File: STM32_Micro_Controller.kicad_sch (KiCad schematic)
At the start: 1 part, among them U1 STM32F103C8T6

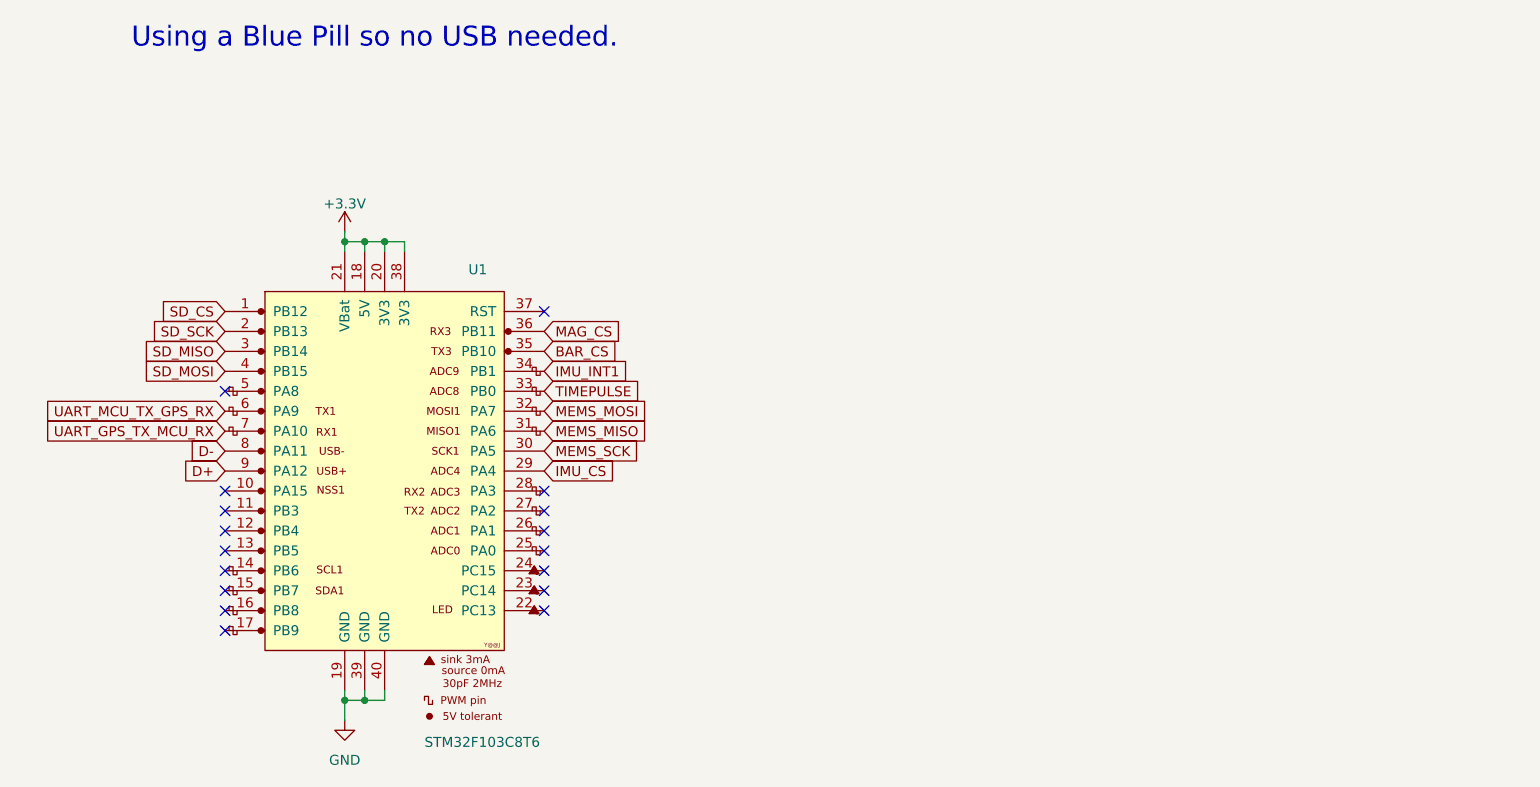
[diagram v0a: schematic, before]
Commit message: Finished the footprint for the Micro Controller
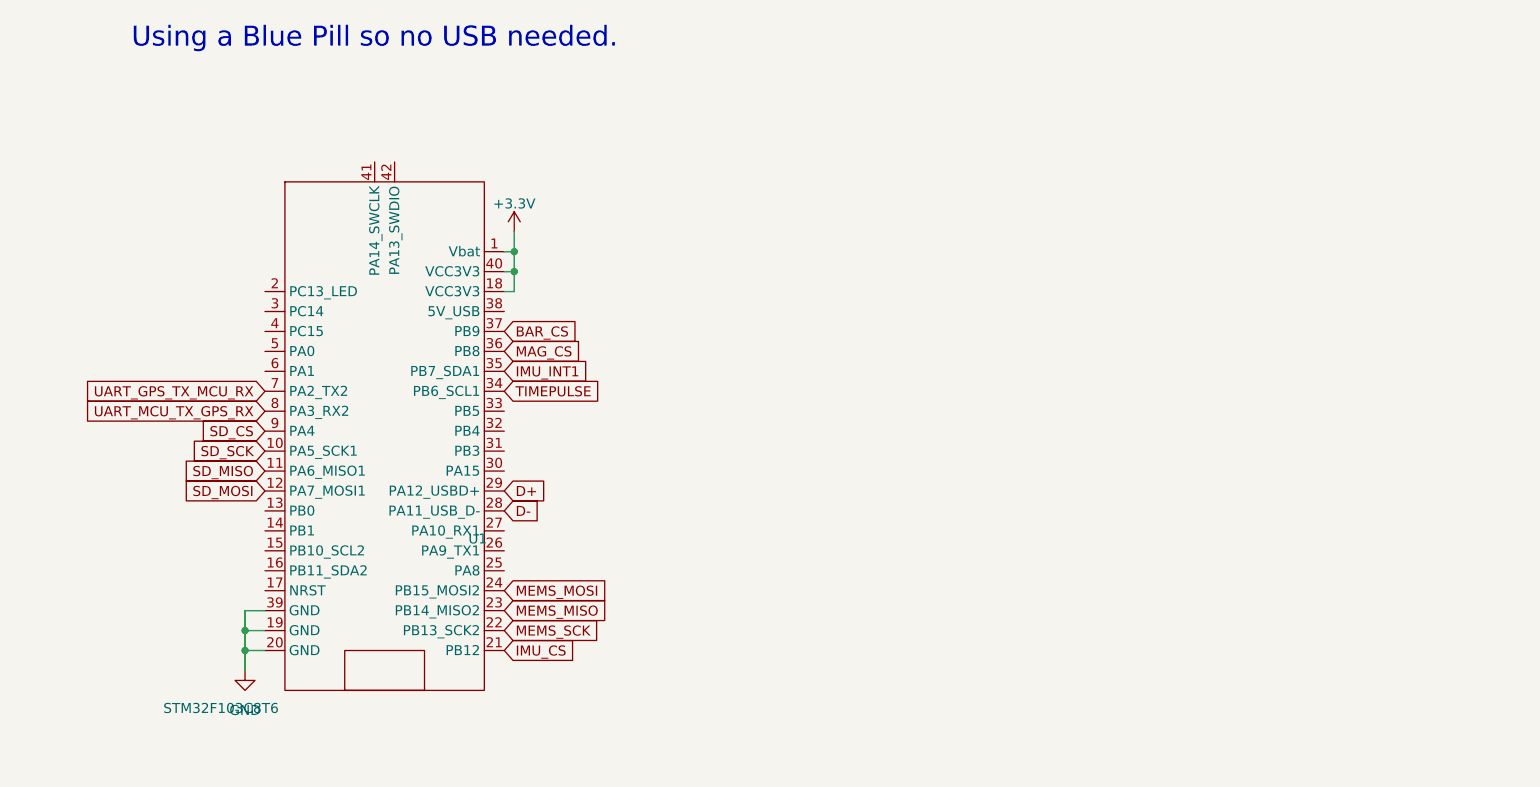
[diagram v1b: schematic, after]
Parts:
- U1: footprint Package_QFP:LQFP-48_7x7mm_P0.5mm -> STM_Pills:YAAJ_BluePill_1; symbol YAAJ_BluePill:YAAJ_BluePill -> bluepill_stm32f103c:BluePill_STM32F103C
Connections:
- net +3.3V: now also U1.1 (Vbat), U1.40 (VCC3V3); no longer U1.20 (3V3), U1.21 (VBat), U1.38 (3V3)
- net BAR_CS: now also U1.37 (PB9); no longer U1.35 (PB10)
- net D+: now also U1.29 (PA12_USBD+); no longer U1.9 (PA12)
- net D-: now also U1.28 (PA11_USB_D-); no longer U1.8 (PA11)
- net GND: now also U1.20 (GND); no longer U1.40 (GND)
- net IMU_CS: now also U1.21 (PB12); no longer U1.29 (PA4)
- net IMU_INT1: now also U1.35 (PB7_SDA1); no longer U1.34 (PB1)
- net MEMS_MISO: now also U1.23 (PB14_MISO2); no longer U1.31 (PA6)
- net MEMS_MOSI: now also U1.24 (PB15_MOSI2); no longer U1.32 (PA7)
- net MEMS_SCK: now also U1.22 (PB13_SCK2); no longer U1.30 (PA5)
- net SD_CS: now also U1.9 (PA4); no longer U1.1 (PB12)
- net SD_MISO: now also U1.11 (PA6_MISO1); no longer U1.3 (PB14)
- net SD_MOSI: now also U1.12 (PA7_MOSI1); no longer U1.4 (PB15)
- net SD_SCK: now also U1.10 (PA5_SCK1); no longer U1.2 (PB13)
- net TIMEPULSE: now also U1.34 (PB6_SCL1); no longer U1.33 (PB0)
- net UART_MCU_TX_GPS_RX: now also U1.8 (PA3_RX2); no longer U1.6 (PA9)
- no-connect marks 17 -> 0

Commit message: Just a few quick edits but only small
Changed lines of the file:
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@@
 		)
 		(property "Value" "STM32F103C8T6"
-			(at 105.156 121.666 0)
+			(at 105.41 124.206 0)
 			(show_name no)
 			(do_not_autoplace no)

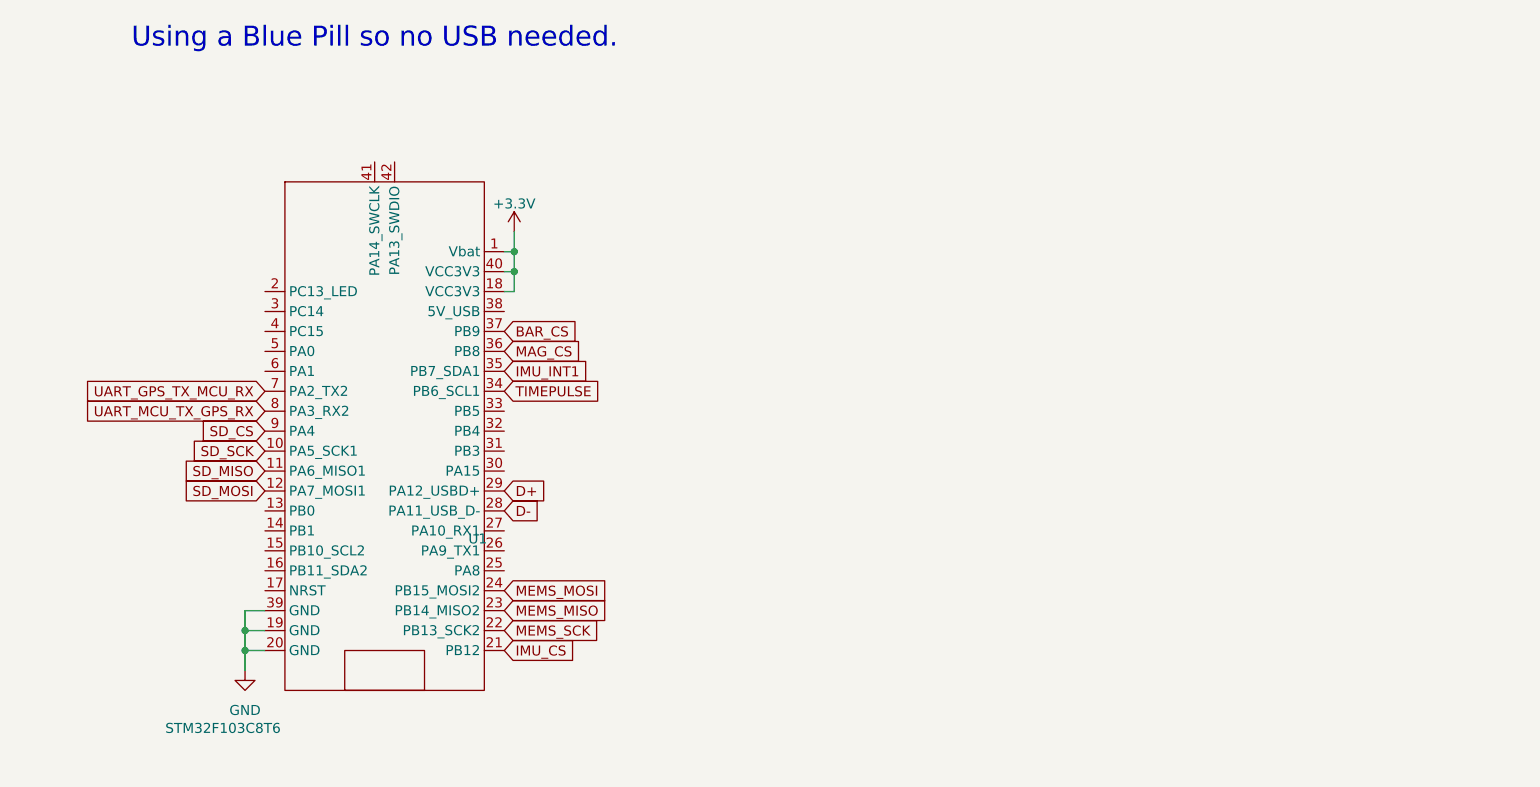
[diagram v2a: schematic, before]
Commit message: Added LEDs to micro controller
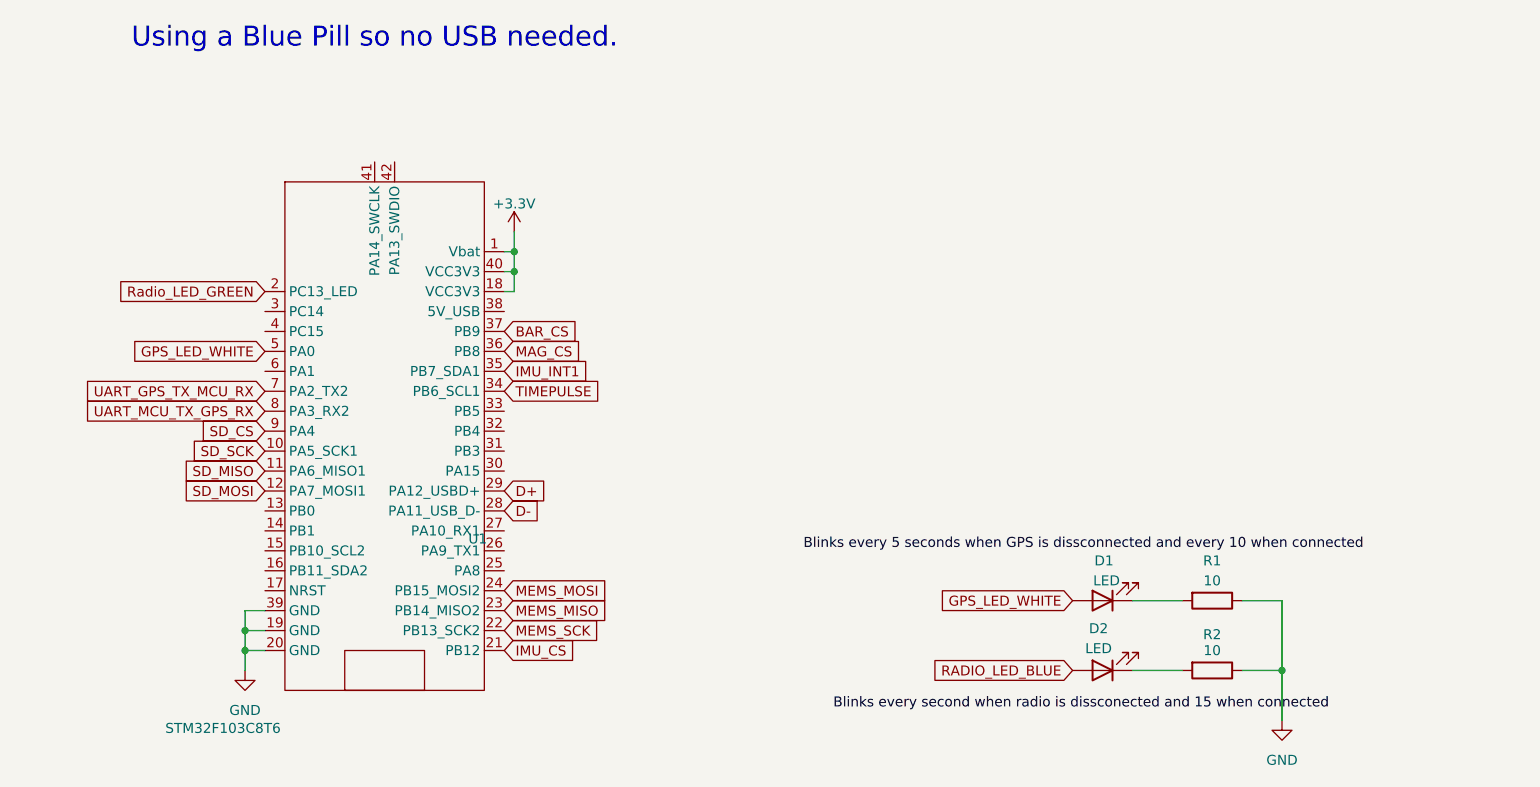
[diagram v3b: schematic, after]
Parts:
- added D1, D2: LED, symbol Device:LED
- added R1, R2: 10, symbol Device:R
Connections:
- net GND: now also R1.1, R2.1
- net Radio_LED_GREEN: now reaches U1.2 (PC13_LED)
- net GPS_LED_WHITE: now reaches U1.5 (PA0)
- net GPS_LED_WHITE: now also D1.2 (A)
- new net: D2.1 (K), R2.2
- new net: D1.1 (K), R1.2
- new net RADIO_LED_BLUE: D2.2 (A)
